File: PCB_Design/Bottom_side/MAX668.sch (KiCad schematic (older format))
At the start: 13 parts, among them U3 MAX668

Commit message: PCB bottom layer populated
PCB bottom layer populated, and waiting for top layer to be merged.
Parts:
- removed CB_MAX_O_3: 68uF, Capacitors_Tantalum_SMD:CP_Tantalum_Case-C_EIA-6032-28_Hand, symbol CP
- added C1, C4: CP, Capacitors_Tantalum_SMD:CP_Tantalum_Case-C_EIA-6032-28_Reflow, symbol CP
- CBMAX_3: footprint Capacitors_Tantalum_SMD:CP_Tantalum_Case-C_EIA-6032-28_Hand -> Capacitors_Tantalum_SMD:CP_Tantalum_Case-C_EIA-6032-28_Reflow
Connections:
- net GND: now also C1.2, C4.2
- net I_out: now also C1.1, C4.1

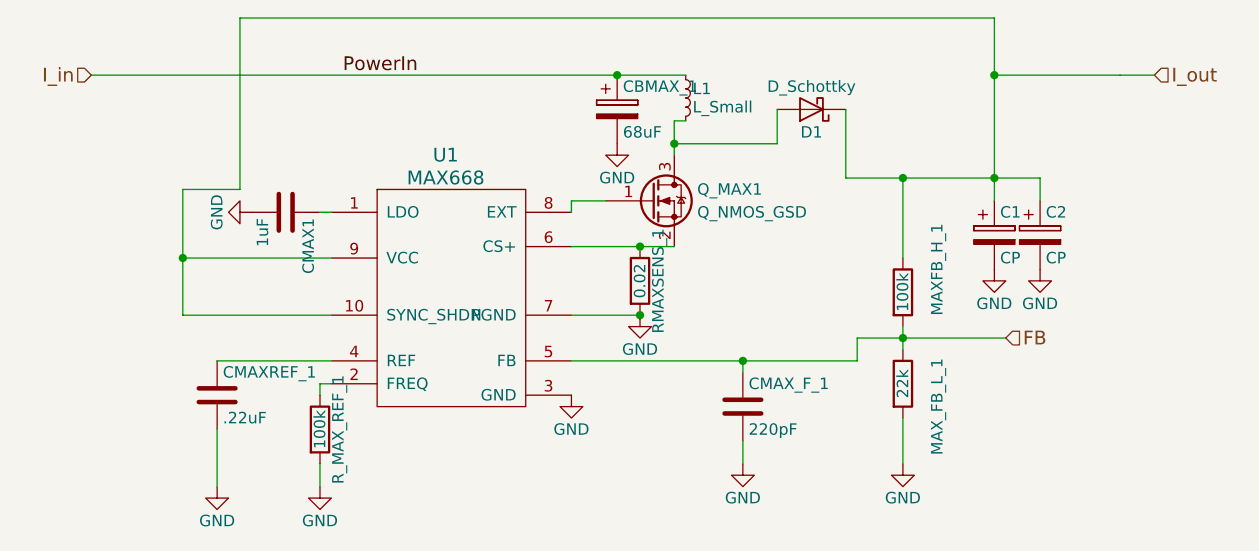
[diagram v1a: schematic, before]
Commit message: Updated PCB structure tree
Full_PCB now includes bottom and top layer hierarchical sheets
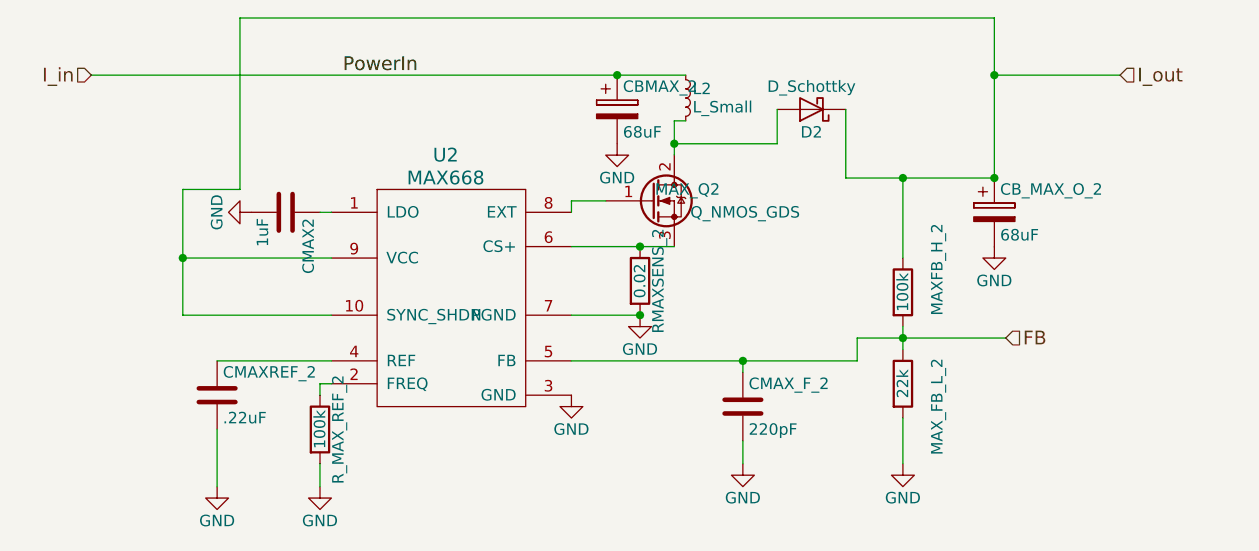
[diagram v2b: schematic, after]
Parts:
- removed C1, C4: CP, Capacitors_Tantalum_SMD:CP_Tantalum_Case-C_EIA-6032-28_Reflow, symbol CP
- removed Q_MAX1: Q_NMOS_GSD, TO_SOT_Packages_SMD:SOT-23, symbol Q_NMOS_GSD
- added CB_MAX_O_3: 68uF, Capacitors_Tantalum_SMD:CP_Tantalum_Case-C_EIA-6032-28_Hand, symbol CP
- added MAX_Q3: Q_NMOS_GDS, TO_SOT_Packages_SMD:TDSON-8-1, symbol Q_NMOS_GDS
- CBMAX_3: footprint Capacitors_Tantalum_SMD:CP_Tantalum_Case-C_EIA-6032-28_Reflow -> Capacitors_Tantalum_SMD:CP_Tantalum_Case-C_EIA-6032-28_Hand
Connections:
- net GND: now also CB_MAX_O_3.2
- net I_out: now also CB_MAX_O_3.1
- net at RMAXSENS_3.1, U3.6 (CS+): now also MAX_Q3.3 (S)
- net at U3.8 (EXT): now also MAX_Q3.1 (G)
- net at D3.2 (A), L3.2: now also MAX_Q3.2 (D)
